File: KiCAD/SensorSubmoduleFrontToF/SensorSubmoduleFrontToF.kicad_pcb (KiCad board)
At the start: 2 copper layers, 18 x 18 mm, 11 parts, among them J1 Conn_01x04_Pin, U1 VL53L0CXV0DH1, U2 AP2112K-3.3

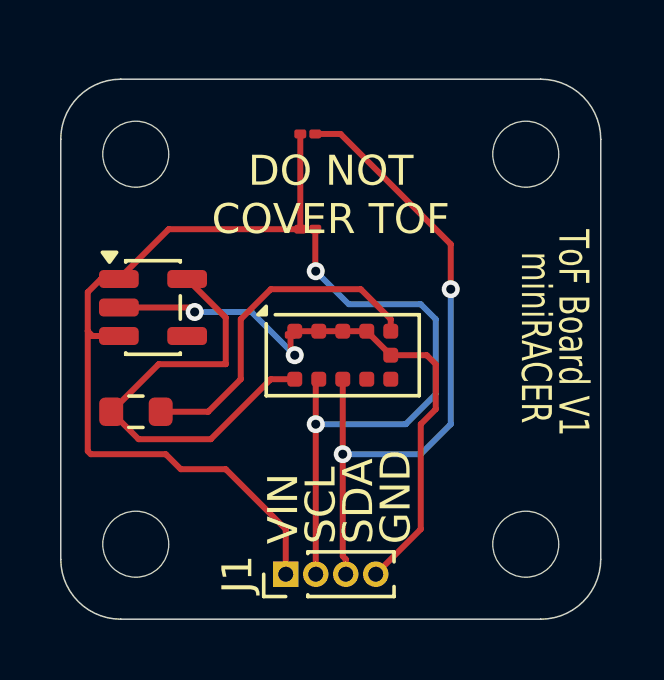
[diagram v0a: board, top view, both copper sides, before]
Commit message: updates to BOM and updates to othere boards (context of kicad pcbs)
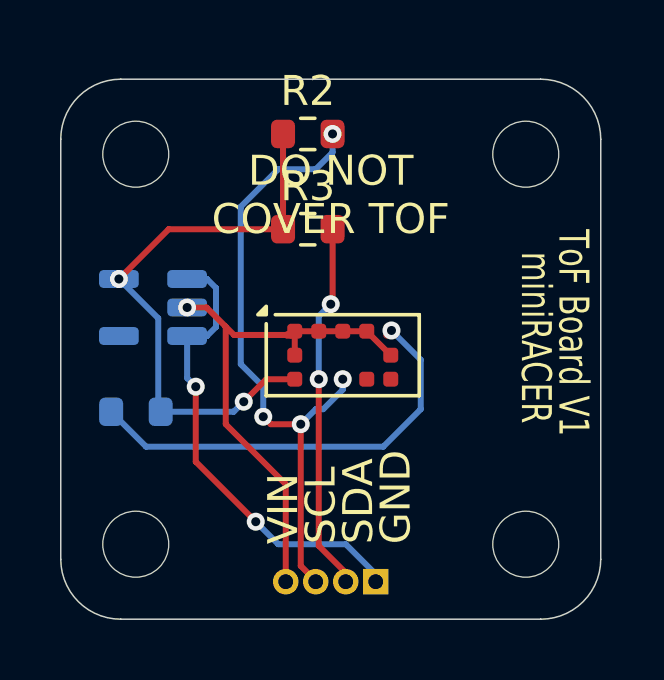
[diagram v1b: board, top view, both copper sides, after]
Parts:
- J1, R1, U2: moved to B.Cu
- R2, R3: footprint Resistor_SMD:R_01005_0402Metric -> Resistor_SMD:R_0603_1608Metric
- moved J1 3.01 mm to (22.5, 28.8)
- moved G*** 0.75 mm to (21.0, 21.5)
- turned R1 to 180 degrees
- turned U2 to 180 degrees
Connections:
- R2 pad 1: Net-(J1-Pin_1) -> Net-(U1-AVDD)
- R3 pad 1: Net-(J1-Pin_1) -> Net-(U1-AVDD)
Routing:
- net Net-(J1-Pin_1): track 26.7 -> 15.6 mm, vias 0 -> 2
- net Net-(J1-Pin_2): track 19.5 -> 12.3 mm
- net Net-(U1-AVDD): track 15.2 -> 19.3 mm, vias 0 -> 2
- net Net-(U1-XSHUT): track 11.3 -> 14.3 mm, vias 0 -> 1
- net Net-(J1-Pin_4): track 20.4 -> 17.7 mm, vias 2 -> 1
- net Net-(J1-Pin_3): track 22.6 -> 20.8 mm, vias 2 -> 4
